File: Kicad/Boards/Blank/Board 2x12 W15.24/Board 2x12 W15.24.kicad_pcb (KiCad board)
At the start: 2 copper layers, 18.8 x 33.2 mm, 1 part, among them J1 Board 2x12 W15.24mm

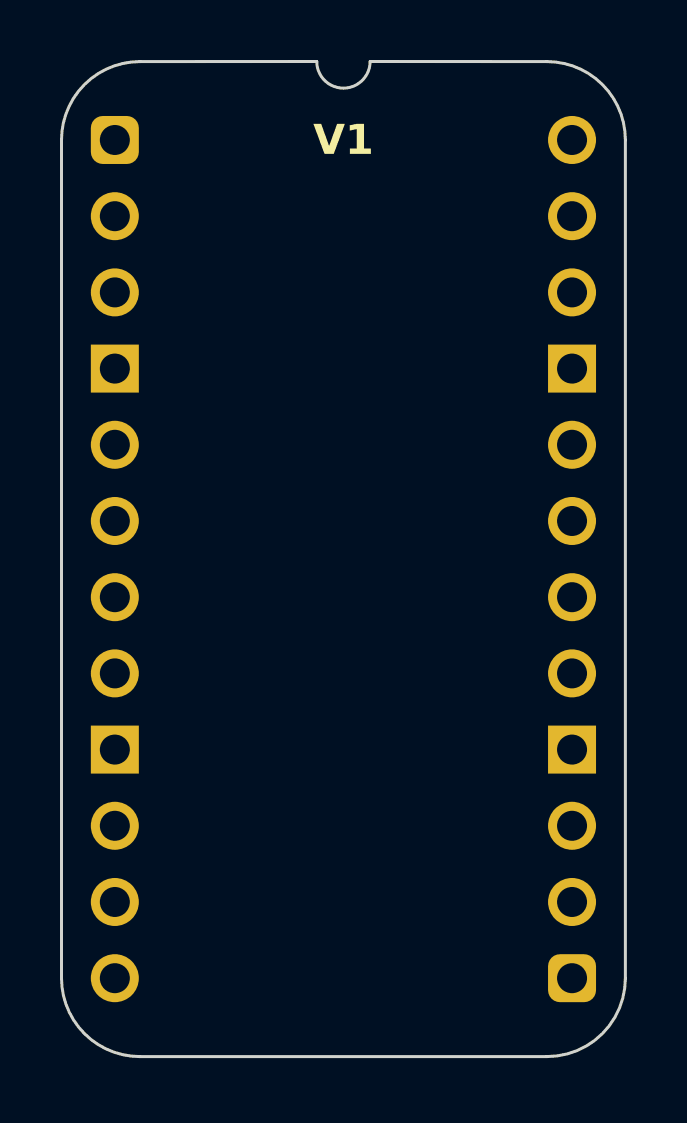
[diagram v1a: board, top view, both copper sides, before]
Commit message: Added silkscreen and power components to some blank boards.
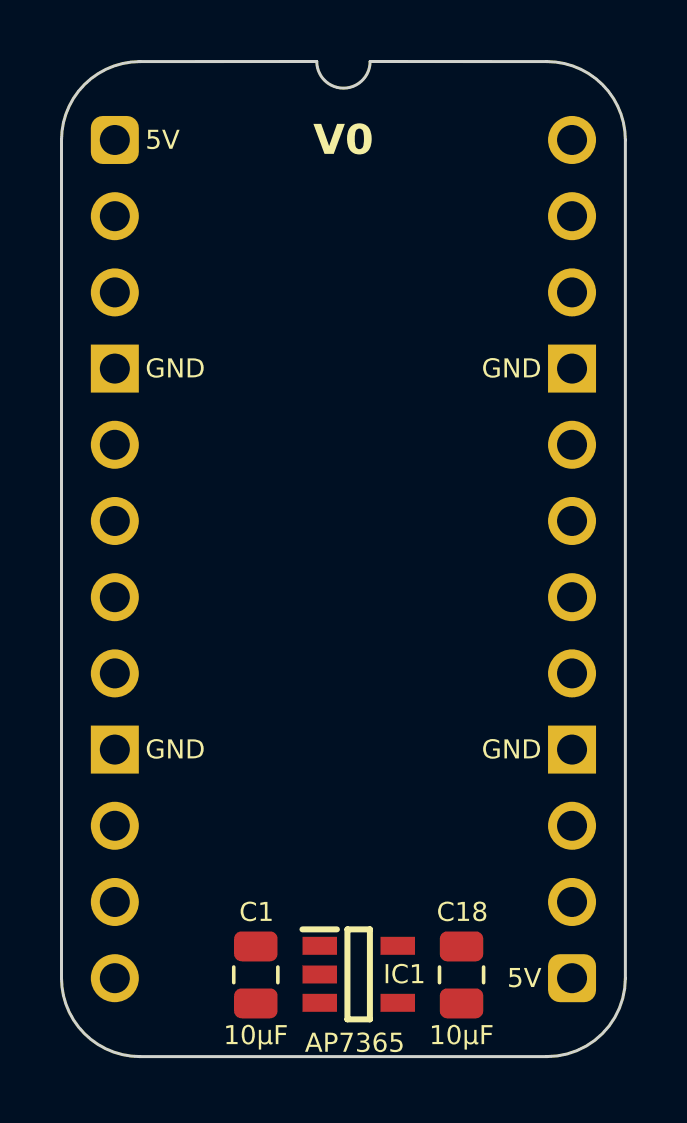
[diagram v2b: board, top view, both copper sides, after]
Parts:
- added C1: 10µF, SamacSys_Parts:C_0805, F.Cu at (4.70, 27.8)
- added C18: 10µF, SamacSys_Parts:C_0805, F.Cu at (11.6, 27.8)
- added IC1: AP7365-33WG-7, SamacSys_Parts:SOT95P285X130-5N, F.Cu at (8.13, 27.8)
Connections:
- J1 pad 1: unconnected-(J1-Pad1) -> 5V
- J1 pad 13: unconnected-(J1-Pad13) -> 5V
- J1 pad 16: unconnected-(J1-Pad16) -> GND
- J1 pad 21: unconnected-(J1-Pad21) -> GND
- J1 pad 4: unconnected-(J1-Pad4) -> GND
- J1 pad 9: unconnected-(J1-Pad9) -> GND
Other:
- board text added: "5V"
- board text added: "GND"
